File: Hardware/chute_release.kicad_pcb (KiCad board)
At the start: 4 copper layers, 20 x 35 mm, 64 parts, among them J1 Conn_01x03, J2 Conn_01x02_Pin, J3 USB4105-GF-A, J4 Conn_01x02, Q1 DMG3415UFY4Q-7, Q2 SSM3K35AMFV_L3F, SW1 SH-7050TB, U1 W25Q128JVS, U2 RP2040, U3 AP2112K-3.3, U4 MCP73831-2-OT, U5 DPS310XTSA1, Y1 ABM8-272-T3

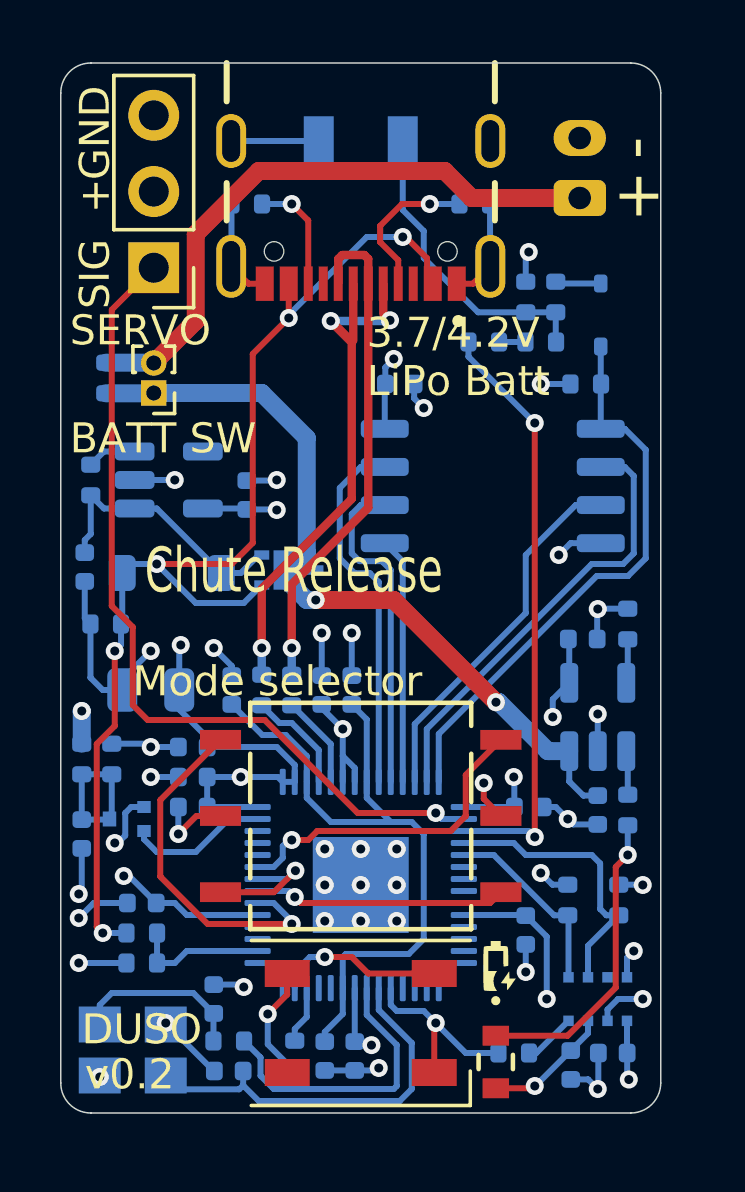
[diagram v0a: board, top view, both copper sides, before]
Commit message: Adjustements of vias and VBATT copper pour
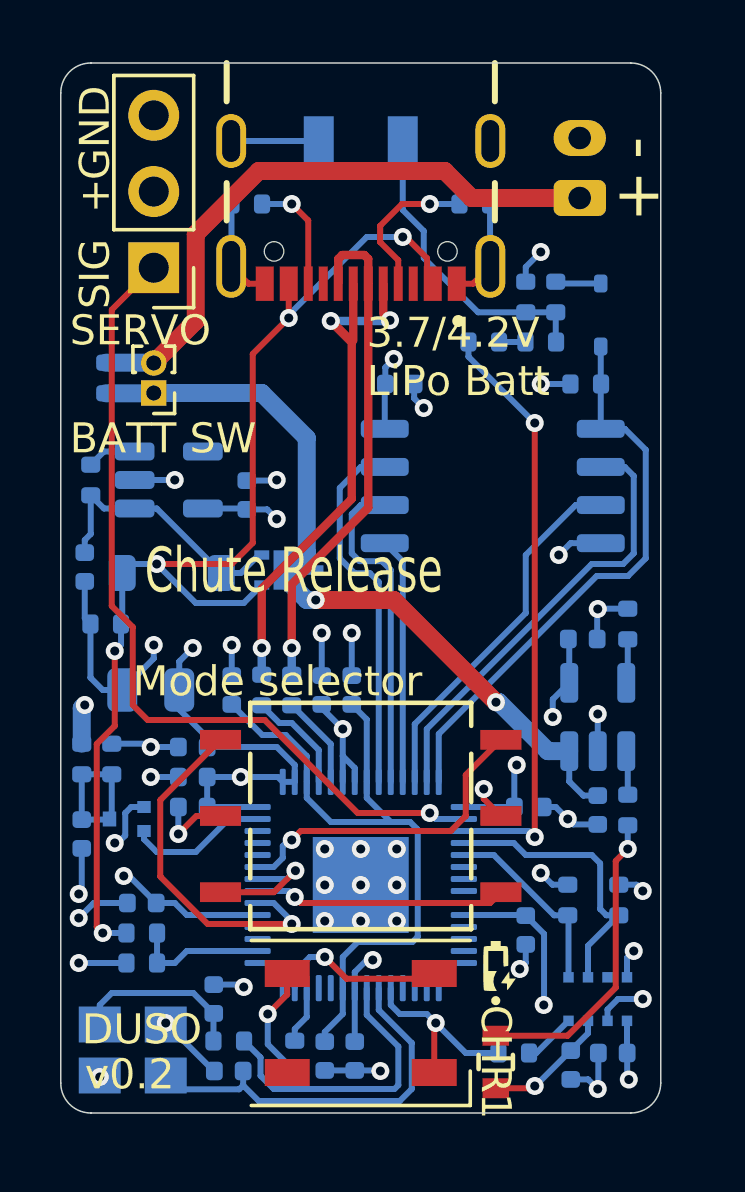
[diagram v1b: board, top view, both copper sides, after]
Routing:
- net +3V3: track 56.0 -> 57.8 mm

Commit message: Swapped GND and PWR planes so GND is closer to BOTTOM. Added 1V1 copper pour
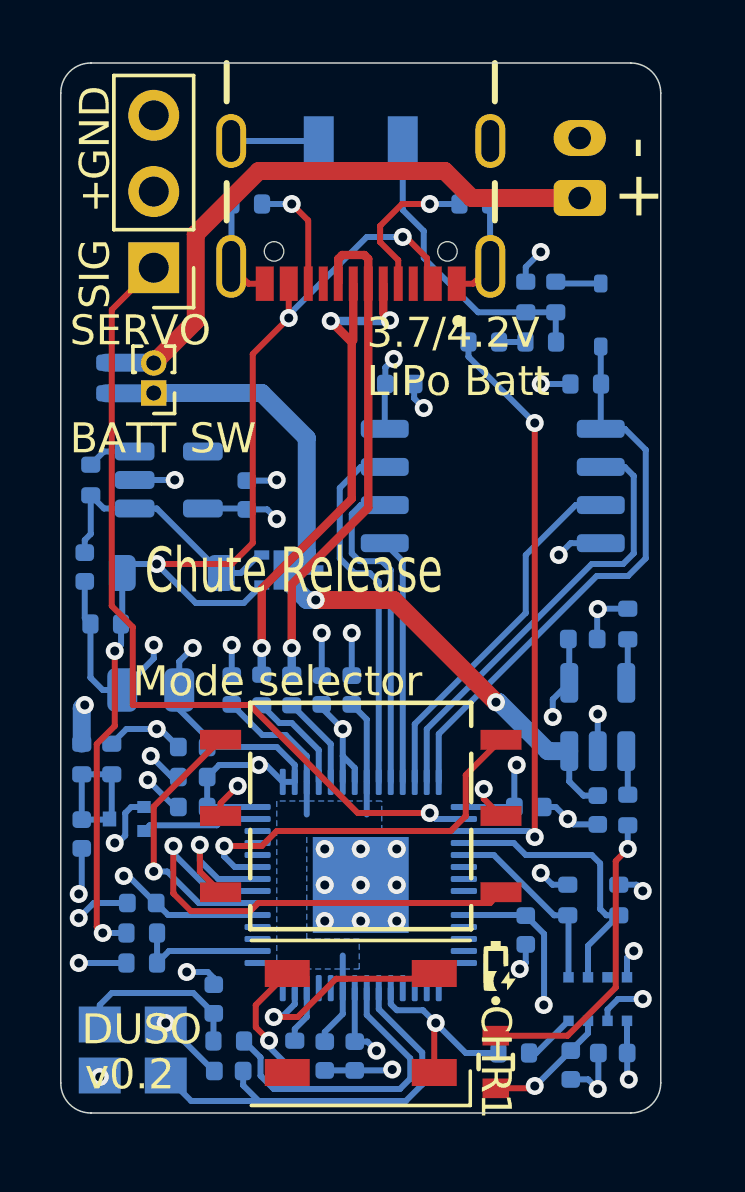
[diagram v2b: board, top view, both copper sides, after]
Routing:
- net +1V1: track 22.6 -> 12.2 mm
- net HEX_SW_2: track 8.43 -> 16.6 mm
- net HEX_SW_1: track 11.9 -> 9.21 mm
- net HEX_SW_8: track 10.9 -> 13.1 mm
- net NEOPIX: track 5.77 -> 7.36 mm
- net GND: track 59.7 -> 61.0 mm, vias 36 -> 37
- net /MCU/XIN: track 13.1 -> 14.2 mm
- net VBAT_SENSE: track 4.69 -> 3.95 mm
- added copper zone on B.Cu, net +1V1
- added copper zone on In1.Cu, net +3V3
- added copper zone on In1.Cu, net +BATT
- added copper zone on In2.Cu, net GND
- removed copper zone on In2.Cu, net +3V3
- removed copper zone on In2.Cu, net +BATT
- removed copper zone on In1.Cu, net GND

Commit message: Changed bat charge current to 100mA
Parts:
- R17: value 5k -> 10k
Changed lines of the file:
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@@
 			)
 		)
-		(property "Value" "5k"
+		(property "Value" "10k"
 			(at -6.2 0.16 90)
 			(layer "B.Fab")

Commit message: Board review fixes
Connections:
- U2 pad 14: /MCU/GPIO11 -> SDO
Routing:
- net SDO: track 1.76 -> 6.08 mm
- net +3V3: track 58.0 -> 58.6 mm

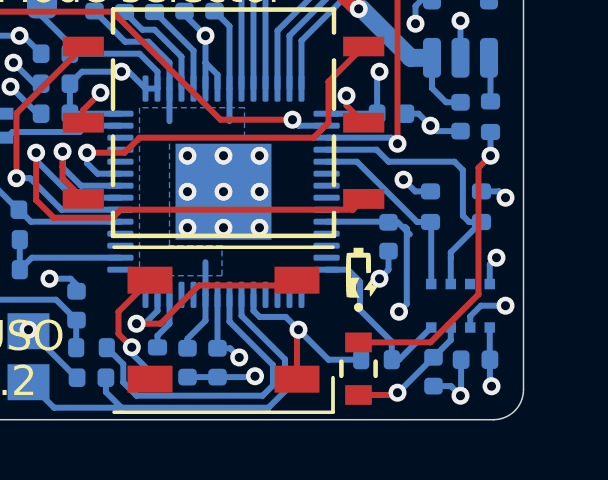
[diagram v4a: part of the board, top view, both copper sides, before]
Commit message: Added silkscreen box to allow board number to be written
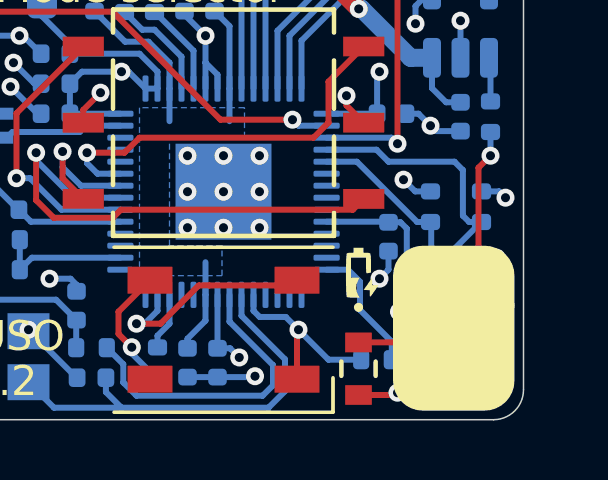
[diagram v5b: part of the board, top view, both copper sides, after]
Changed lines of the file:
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@@
 		)
 		(property "Value" "TLMS1100-GS08"
-			(at -0.5 2.5 270)
+			(at -0.5 2.5 -90)
 			(unlocked yes)
 			(layer "F.Fab")
@@
 		)
 		(fp_text user "${REFERENCE}"
-			(at 0 -1.5 270)
+			(at 0 -1.5 -90)
 			(unlocked yes)
 			(layer "F.Fab")
@@
 		)
 	)
-	(gr_text "v0.2"
+	(gr_text "v0.2\n"
 		(at 117.3 115.9 0)
 		(layer "F.SilkS")
@@
 			(justify left bottom)
 		)
-		(render_cache "v0.2" 0
+		(render_cache "v0.2\n" 0
 			(polygon
 				(pts
@@
 	)
 	(segment
-		(start 132 110.02)
-		(end 132.309999 110.02)
-		(width 0.2)
-		(layer "B.Cu")
-		(net 5)
-	)
-	(segment
 		(start 126.3 112.4375)
 		(end 126.3 114.22)
@@
 	)
 	(segment
-		(start 132.309999 110.02)
-		(end 132.711121 110.421122)
-		(width 0.2)
-		(layer "B.Cu")
-		(net 5)
-	)
-	(segment
 		(start 125.2 102.98)
 		(end 125.2 103.1)
@@
 	)
 	(segment
-		(start 132.55 110.168745)
-		(end 132.61 110.228745)
-		(width 0.2)
-		(layer "B.Cu")
-		(net 5)
-	)
-	(segment
 		(start 118.756134 108.7)
 		(end 119.656134 109.6)
@@
 	)
 	(segment
+		(start 132.401255 110.02)
+		(end 132.61 110.228745)
+		(width 0.2)
+		(layer "B.Cu")
+		(net 5)
+	)
+	(segment
 		(start 135.69 108.99)
 		(end 135.9 109.2)
@@
 	)
 	(segment
+		(start 132 110.02)
+		(end 132.401255 110.02)
+		(width 0.2)
+		(layer "B.Cu")
+		(net 5)
+	)
+	(segment
 		(start 123.0625 106.4)
 		(end 121.38 106.4)
@@
 			)
 		)
+	)
+	(zone
+		(net 0)
+		(net_name "")
+		(layer "F.SilkS")
+		(hatch full 0.5)
+		(connect_pads
+			(clearance 0.5)
+		)
+		(min_thickness 0.25)
+		(filled_areas_thickness no)
+		(fill yes
+			(thermal_gap 0.5)
+			(thermal_bridge_width 0.5)
+			(smoothing fillet)
+			(radius 1)
+		)
+		(polygon
+			(pts
+				(xy 132.15 116.3) (xy 136.2 116.3) (xy 136.2 110.8) (xy 132.15 110.8)
+			)
+		)

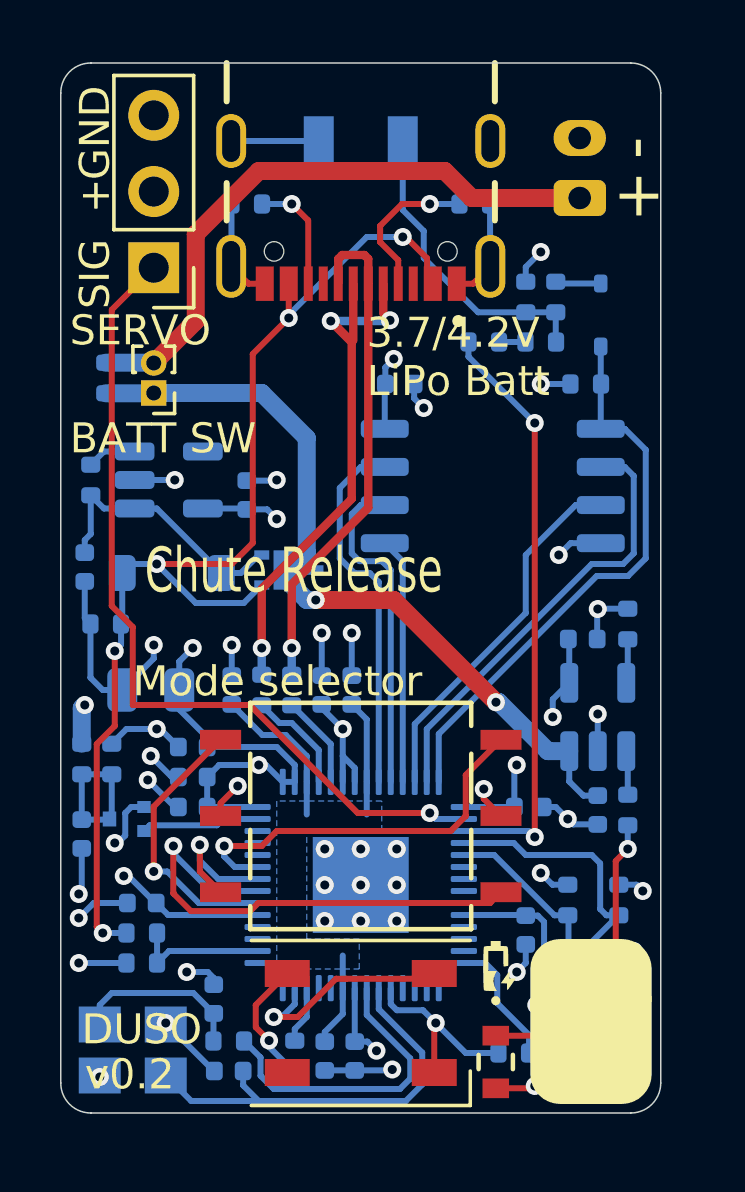
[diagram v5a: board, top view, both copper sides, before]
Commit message: Changed bat sw footprint to header 2.54mm pitch. Adjusted silkscreens.
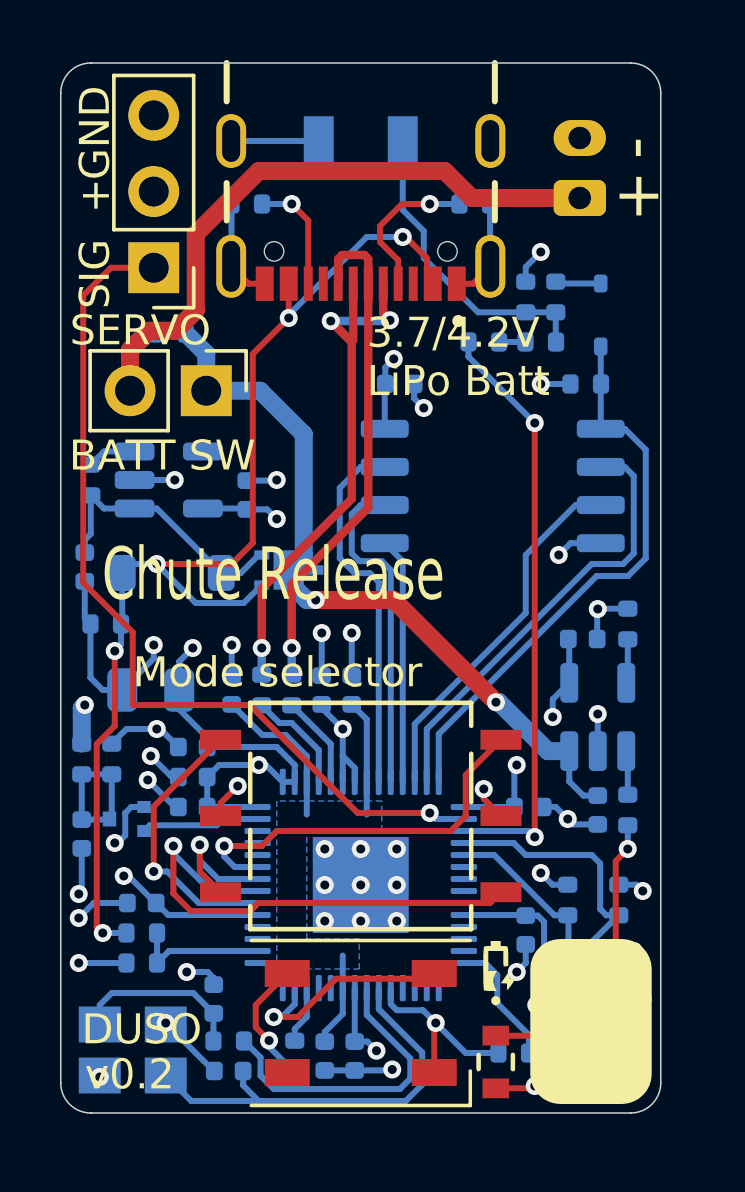
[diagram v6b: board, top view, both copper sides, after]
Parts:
- J4: footprint Connector_PinHeader_1.00mm:PinHeader_1x02_P1.00mm_Vertical -> Connector_PinHeader_2.54mm:PinHeader_1x02_P2.54mm_Vertical
- moved R23 2.62 mm to (120.2, 90.6), turned to 0 degrees
- moved J4 1.75 mm to (121.3, 92.5), turned to -90 degrees
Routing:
- net Net-(J2-Pin_1): track 20.5 -> 23.1 mm
- net /MCU/GPIO0: track 28.1 -> 29.7 mm
- net +BATT: track 27.6 -> 26.4 mm
